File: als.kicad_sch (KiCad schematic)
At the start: 3 parts, among them J11 Conn_02x12_Odd_Even, U14 TCA9802, U16 MIC5365-3.0YD5-TR

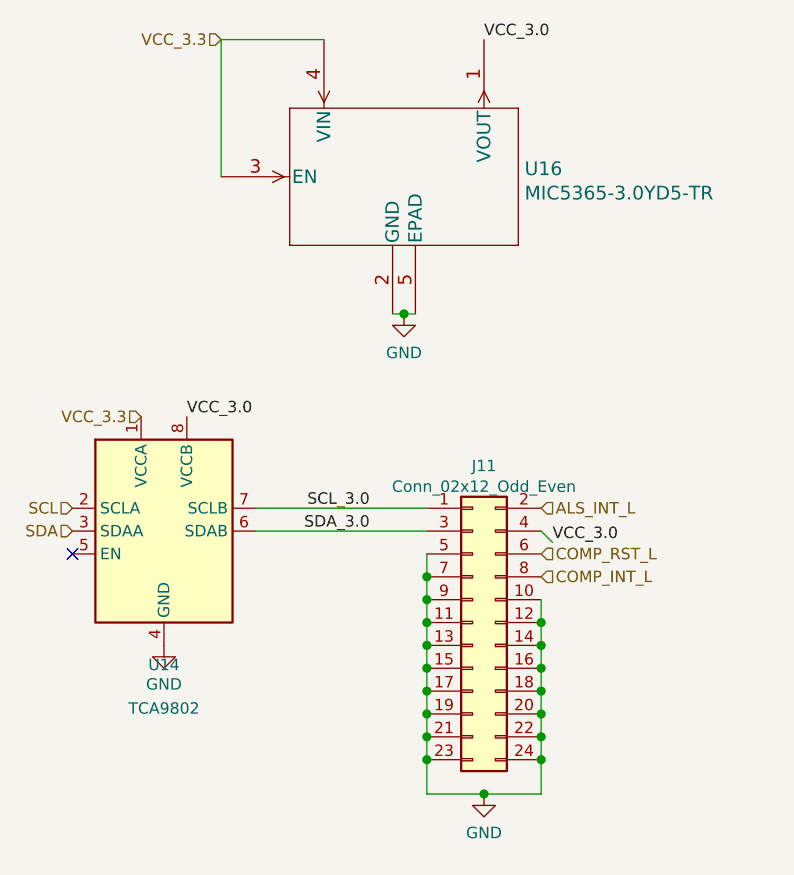
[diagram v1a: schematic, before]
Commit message: Wire GT9110 INT pin to a GPIO, wire ARM_RST and Wake pins to test points instead of GPIOs. Add lots of test points, and footprints for status/power LEDs.
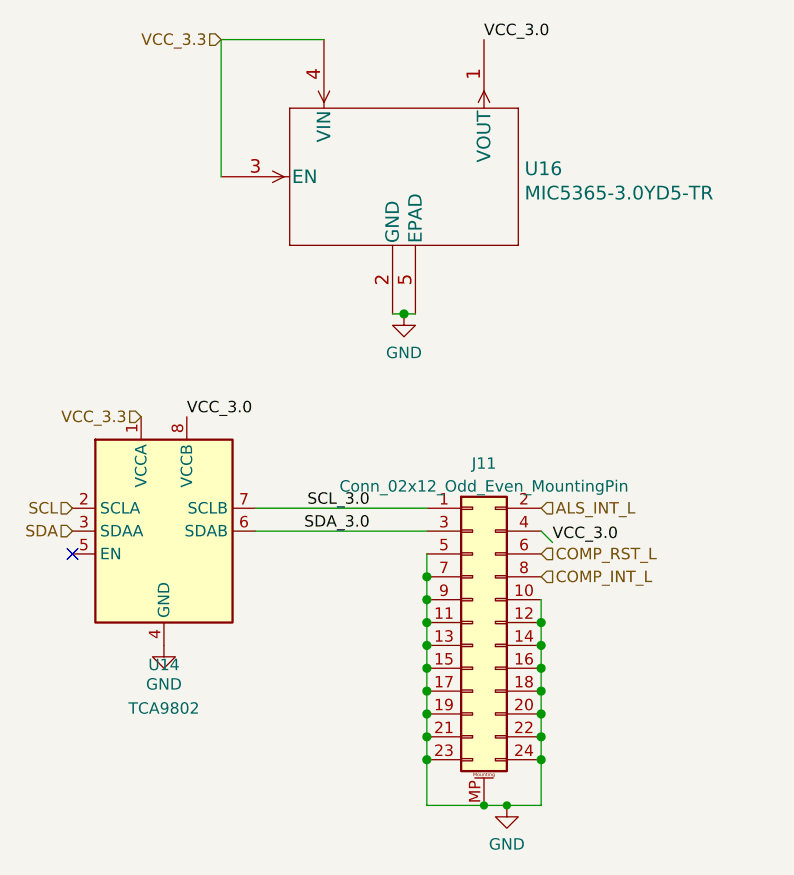
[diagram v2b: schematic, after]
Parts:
- J11: value Conn_02x12_Odd_Even -> Conn_02x12_Odd_Even_MountingPin; symbol Connector_Generic:Conn_02x12_Odd_Even -> Connector_Generic_MountingPin:Conn_02x12_Odd_Even_MountingPin
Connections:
- net GND: now also J11.MP (MountPin)
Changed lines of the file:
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@@
   (junction (at 140.97 102.87) (diameter 1.016) (color 0 0 0 0)
   )
+  (junction (at 137.16 113.03) (diameter 0) (color 0 0 0 0)
+  )
   (junction (at 128.27 105.41) (diameter 1.016) (color 0 0 0 0)
   )
@@
   (junction (at 128.27 90.17) (diameter 1.016) (color 0 0 0 0)
   )
+  (junction (at 134.62 113.03) (diameter 0) (color 0 0 0 0)
+  )
   (junction (at 140.97 95.25) (diameter 1.016) (color 0 0 0 0)
   )
@@
   )
   (junction (at 140.97 105.41) (diameter 1.016) (color 0 0 0 0)
-  )
-  (junction (at 134.62 111.76) (diameter 1.016) (color 0 0 0 0)
   )
   (junction (at 128.27 97.79) (diameter 1.016) (color 0 0 0 0)
@@
     (stroke (width 0) (type solid) (color 0 0 0 0))
   )
-  (wire (pts (xy 128.27 107.95) (xy 128.27 111.76))
-    (stroke (width 0) (type solid) (color 0 0 0 0))
-  )
-  (wire (pts (xy 128.27 111.76) (xy 134.62 111.76))
+  (wire (pts (xy 128.27 107.95) (xy 128.27 113.03))
+    (stroke (width 0) (type solid) (color 0 0 0 0))
+  )
+  (wire (pts (xy 128.27 113.03) (xy 134.62 113.03))
     (stroke (width 0) (type solid) (color 0 0 0 0))
   )
@@
     (stroke (width 0) (type solid) (color 0 0 0 0))
   )
-  (wire (pts (xy 140.97 107.95) (xy 140.97 111.76))
-    (stroke (width 0) (type solid) (color 0 0 0 0))
-  )
-  (wire (pts (xy 140.97 111.76) (xy 134.62 111.76))
+  (wire (pts (xy 140.97 107.95) (xy 140.97 113.03))
+    (stroke (width 0) (type solid) (color 0 0 0 0))
+  )
+  (wire (pts (xy 140.97 113.03) (xy 137.16 113.03))
+    (stroke (width 0) (type solid) (color 0 0 0 0))
+  )
+  (wire (pts (xy 137.16 113.03) (xy 134.62 113.03))
     (stroke (width 0) (type solid) (color 0 0 0 0))
   )
@@
     (pin "1")
   )
-  (symbol (lib_id "power:GND") (at 134.62 111.76 0) (unit 1)
-    (in_bom yes) (on_board yes) (fields_autoplaced)
-    (property "Reference" "#PWR0125" (id 0) (at 134.62 118.11 0)
-      (effects (font (size 1.27 1.27)) hide)
-    )
-    (property "Value" "GND" (id 1) (at 134.62 116.0844 0))
-    (property "Footprint" "" (id 2) (at 134.62 111.76 0)
-      (effects (font (size 1.27 1.27)) hide)
-    )
-    (property "Datasheet" "" (id 3) (at 134.62 111.76 0)
+  (symbol (lib_id "power:GND") (at 137.16 113.03 0) (unit 1)
+    (in_bom yes) (on_board yes) (fields_autoplaced)
+    (property "Reference" "#PWR0125" (id 0) (at 137.16 119.38 0)
+      (effects (font (size 1.27 1.27)) hide)
+    )
+    (property "Value" "GND" (id 1) (at 137.16 117.3544 0))
+    (property "Footprint" "" (id 2) (at 137.16 113.03 0)
+      (effects (font (size 1.27 1.27)) hide)
+    )
+    (property "Datasheet" "" (id 3) (at 137.16 113.03 0)
       (effects (font (size 1.27 1.27)) hide)
     )
@@
     (pin "1")
   )
-  (symbol (lib_id "Connector_Generic:Conn_02x12_Odd_Even") (at 133.35 92.71 0) (unit 1)
-    (in_bom yes) (on_board yes) (fields_autoplaced)
-    (property "Reference" "J11" (id 0) (at 134.62 75.3068 0))
-    (property "Value" "Conn_02x12_Odd_Even" (id 1) (at 134.62 77.6055 0))
+  (symbol (lib_id "Connector_Generic_MountingPin:Conn_02x12_Odd_Even_MountingPin") (at 133.35 92.71 0) (unit 1)
+    (in_bom yes) (on_board yes) (fields_autoplaced)
+    (property "Reference" "J11" (id 0) (at 134.62 75.0402 0))
+    (property "Value" "Conn_02x12_Odd_Even_MountingPin" (id 1) (at 134.62 77.5771 0))
     (property "Footprint" "footprints:AA03-S024VA1" (id 2) (at 133.35 92.71 0)
       (effects (font (size 1.27 1.27)) hide)
@@
     (pin "8")
     (pin "9")
+    (pin "MP")
   )
   (symbol (lib_id "Interface:TCA9802") (at 99.06 82.55 0) (unit 1)
